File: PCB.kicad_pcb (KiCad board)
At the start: 2 copper layers, 88.5 x 156.5 mm, 48 parts, among them J1 Conn_01x04, J3 Screw_Terminal_01x05, J4 Screw_Terminal_01x05, K1 G5LE-1A_DC3, K2 G5LE-1A_DC3, K3 G5LE-1, K4 G5LE-1, K6 G5LE-1, K7 G5LE-1A_DC3, Q1 DMN65D8L-7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

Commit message: update the pcb
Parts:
- removed C2: 10uF, Capacitor_SMD:C_0603_1608Metric
- removed J1: Conn_01x04, Connector_PinHeader_2.54mm:PinHeader_1x04_P2.54mm_Horizontal
- removed J3, J4: Screw_Terminal_01x05, 1x5 screw conn:1935190
- added C_10uF_2: 10uF, Capacitor_SMD:C_0603_1608Metric, B.Cu at (62.0, 82.0)
- added J_LCDconn_1: Conn_01x04, Connector_PinHeader_2.54mm:PinHeader_1x04_P2.54mm_Horizontal, F.Cu at (65.5, 80.5)
- added J_VFDconnectors_2: Screw_Terminal_01x05, 1x5 screw conn:1935190, F.Cu at (93.2, 214.5)
- added J_VFDconnectors_3: Screw_Terminal_01x05, 1x5 screw conn:1935190, F.Cu at (121.5, 214.5)

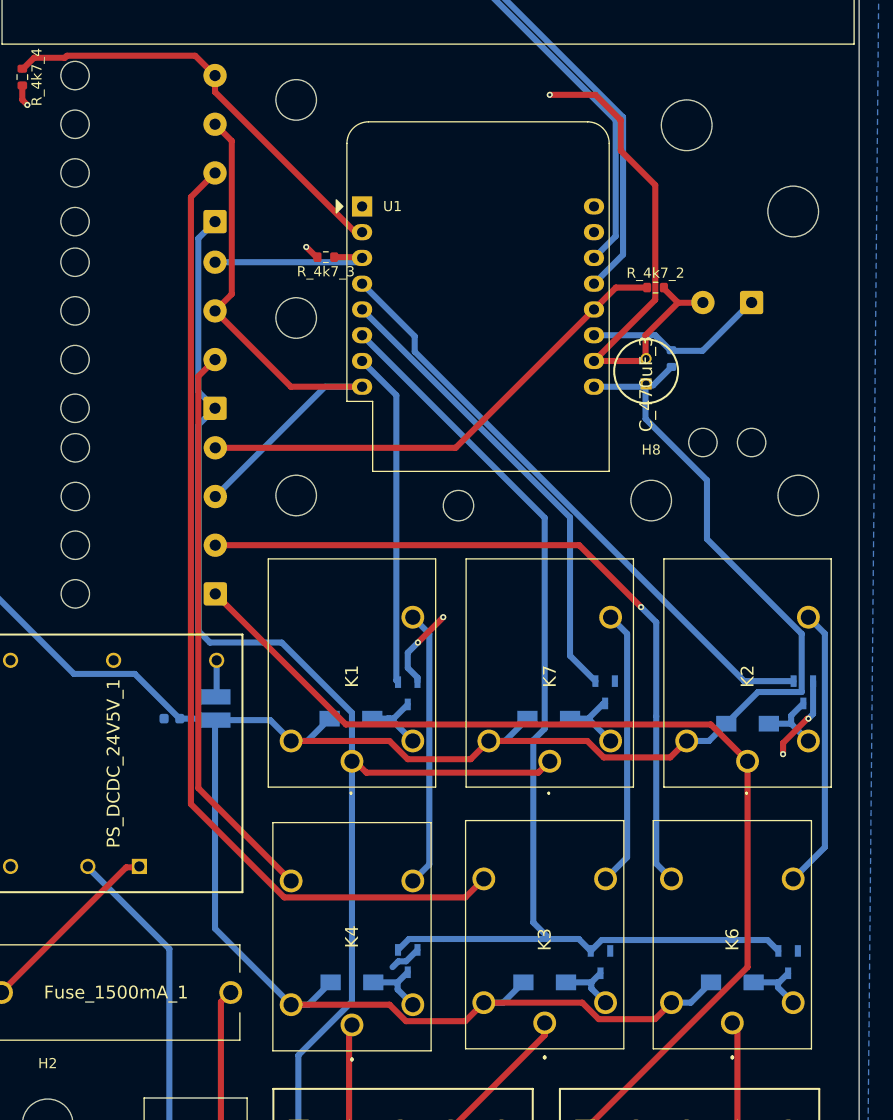
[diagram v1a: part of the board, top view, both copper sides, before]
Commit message: finalni uprava nazvu na pcb
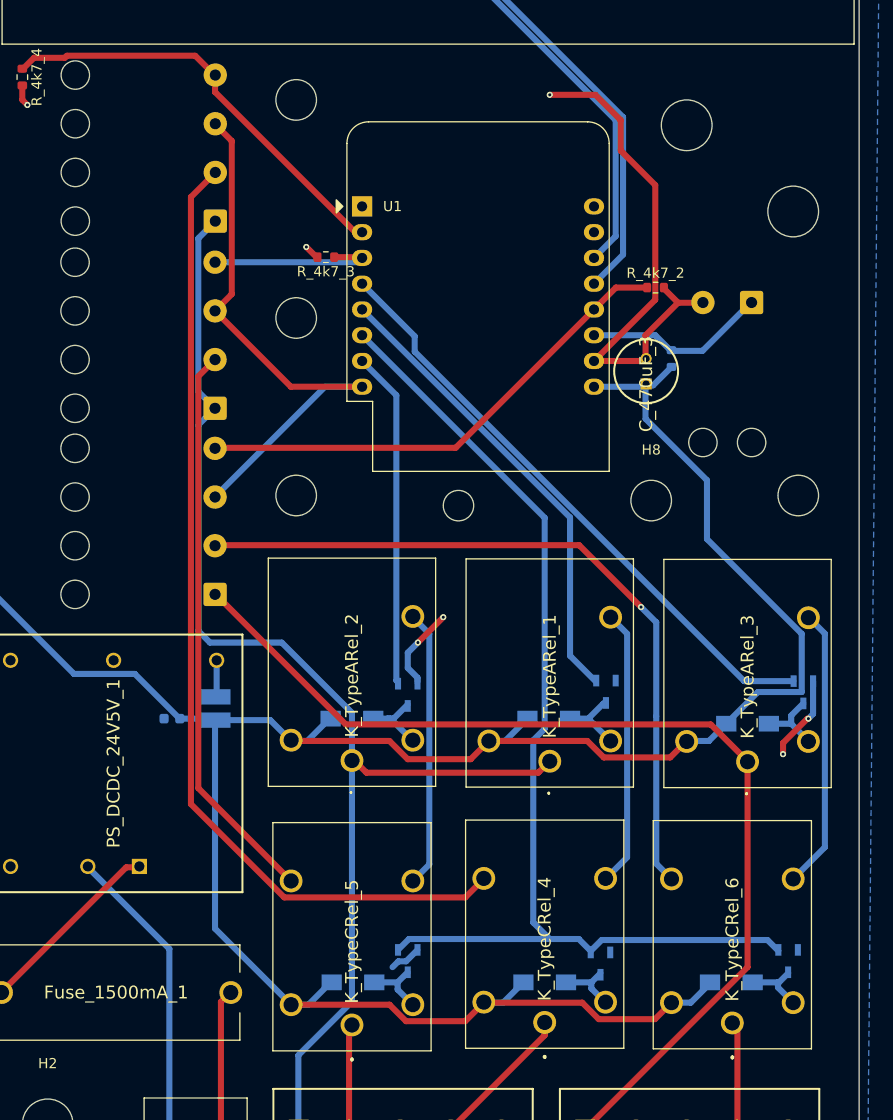
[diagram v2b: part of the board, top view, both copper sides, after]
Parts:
- removed D1, D2, D3, D4, D5, D6: SK16, schottky:DIOM5027X250N
- removed K1, K2, K7: G5LE-1A_DC3, type a relay:G5LE1A4DC5
- removed K3, K4, K6: G5LE-1, type c relay:G5LE1DC3
- removed Q1, Q2, Q3, Q4, Q5, Q6: DMN65D8L-7, mosfet:SOT96P240X115-3N
- removed SW1: Local DI0 (onoff), Connector_Wire:SolderWire-0.5sqmm_1x04_P4.8mm_D0.9mm_OD2.3mm_Relief
- removed SW3: Local DI2 (decspeed), Connector_Wire:SolderWire-0.5sqmm_1x04_P4.8mm_D0.9mm_OD2.3mm_Relief
- removed SW5: Local DI1 (incspeed), Connector_Wire:SolderWire-0.5sqmm_1x04_P4.8mm_D0.9mm_OD2.3mm_Relief
- added D_schottky_1: SK16, schottky:DIOM5027X250N, B.Cu at (117.5, 200.0)
- added D_schottky_2: SK16, schottky:DIOM5027X250N, B.Cu at (98.6, 200.0)
- added D_schottky_3: SK16, schottky:DIOM5027X250N, B.Cu at (135.9, 200.0)
- added D_schottky_4: SK16, schottky:DIOM5027X250N, B.Cu at (117.9, 174.0)
- added D_schottky_5: SK16, schottky:DIOM5027X250N, B.Cu at (98.5, 174.0)
- added D_schottky_6: SK16, schottky:DIOM5027X250N, B.Cu at (137.5, 174.5)
- added K_TypeARel_1: G5LE-1A_DC3, type a relay:G5LE1A4DC5, F.Cu at (118.0, 178.2)
- added K_TypeARel_2: G5LE-1A_DC3, type a relay:G5LE1A4DC5, F.Cu at (98.5, 178.1)
- added K_TypeARel_3: G5LE-1A_DC3, type a relay:G5LE1A4DC5, F.Cu at (137.5, 178.2)
- added K_TypeCRel_4: G5LE-1, type c relay:G5LE1DC3, F.Cu at (117.5, 203.9)
- added K_TypeCRel_5: G5LE-1, type c relay:G5LE1DC3, F.Cu at (98.5, 204.2)
- added K_TypeCRel_6: G5LE-1, type c relay:G5LE1DC3, F.Cu at (136.0, 204.0)
- added Q_NchMOSFET_1: DMN65D8L-7, mosfet:SOT96P240X115-3N, B.Cu at (123.0, 198.2)
- added Q_NchMOSFET_2: DMN65D8L-7, mosfet:SOT96P240X115-3N, B.Cu at (104.0, 197.9)
- added Q_NchMOSFET_3: DMN65D8L-7, mosfet:SOT96P240X115-3N, B.Cu at (141.5, 197.9)
- added Q_NchMOSFET_4: DMN65D8L-7, mosfet:SOT96P240X115-3N, B.Cu at (123.5, 171.3)
- added Q_NchMOSFET_5: DMN65D8L-7, mosfet:SOT96P240X115-3N, B.Cu at (104.0, 171.7)
- added Q_NchMOSFET_6: DMN65D8L-7, mosfet:SOT96P240X115-3N, B.Cu at (143.0, 171.4)
- added SW_DecSpeed_4: Local DI2 (decspeed), Connector_Wire:SolderWire-0.5sqmm_1x04_P4.8mm_D0.9mm_OD2.3mm_Relief, B.Cu at (85.0, 161.8)
- added SW_IncSpeed_3: Local DI1 (incspeed), Connector_Wire:SolderWire-0.5sqmm_1x04_P4.8mm_D0.9mm_OD2.3mm_Relief, B.Cu at (85.0, 143.4)
- added SW_OnOff_2: Local DI0 (onoff), Connector_Wire:SolderWire-0.5sqmm_1x04_P4.8mm_D0.9mm_OD2.3mm_Relief, B.Cu at (85.0, 125.0)
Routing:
- net Net-(D_schottky_5-A): track 0.00 -> 7.49 mm
- net Net-(D5-A): track 7.49 -> 0.00 mm
- net Net-(D_schottky_4-A): track 0.00 -> 7.19 mm
- net Net-(D4-A): track 7.19 -> 0.00 mm
- net Net-(D_schottky_6-A): track 0.00 -> 7.10 mm
- net Net-(D6-A): track 7.10 -> 0.00 mm
- net Net-(D_schottky_2-A): track 0.00 -> 6.64 mm
- net Net-(D2-A): track 6.64 -> 0.00 mm
- net Net-(D_schottky_3-A): track 0.00 -> 6.39 mm
- net Net-(D3-A): track 6.39 -> 0.00 mm
- net Net-(D_schottky_1-A): track 0.00 -> 6.35 mm
- net Net-(D1-A): track 6.35 -> 0.00 mm

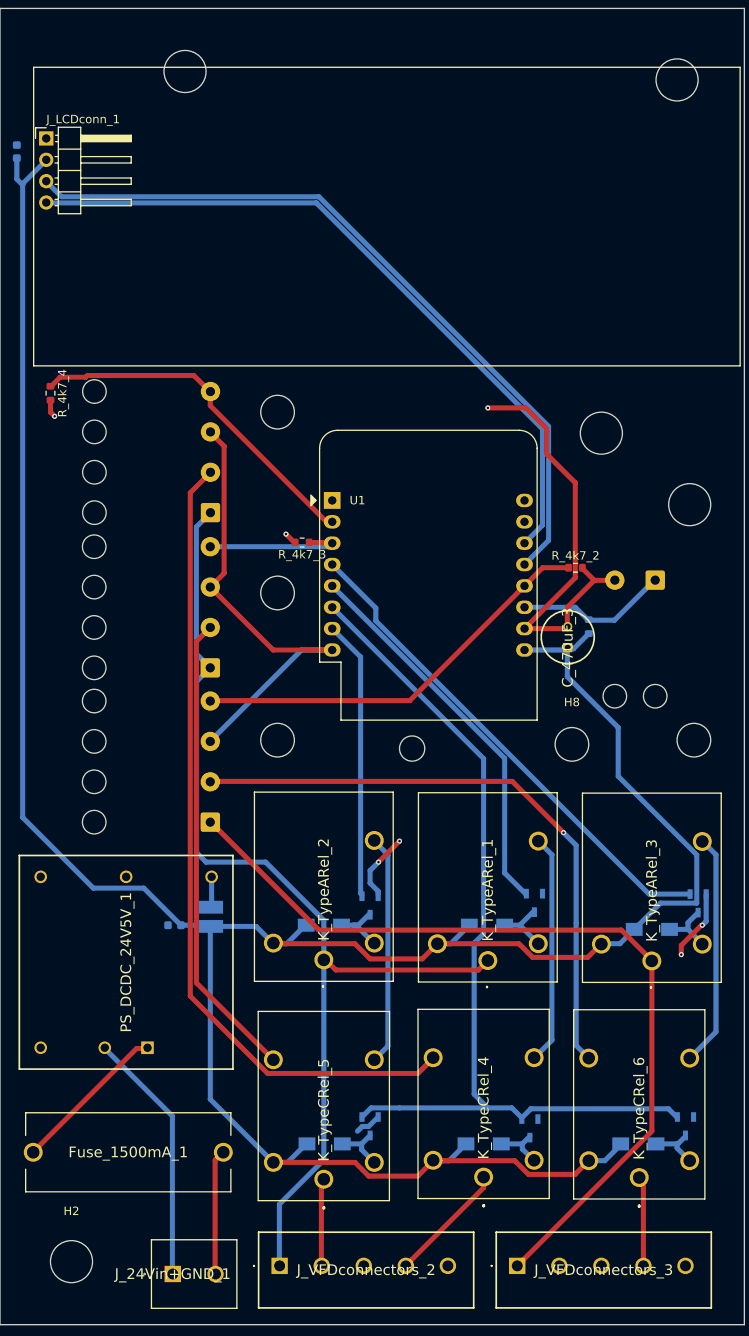
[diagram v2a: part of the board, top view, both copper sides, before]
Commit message: uprava textu na pcb aby byl videt i pod komponenty
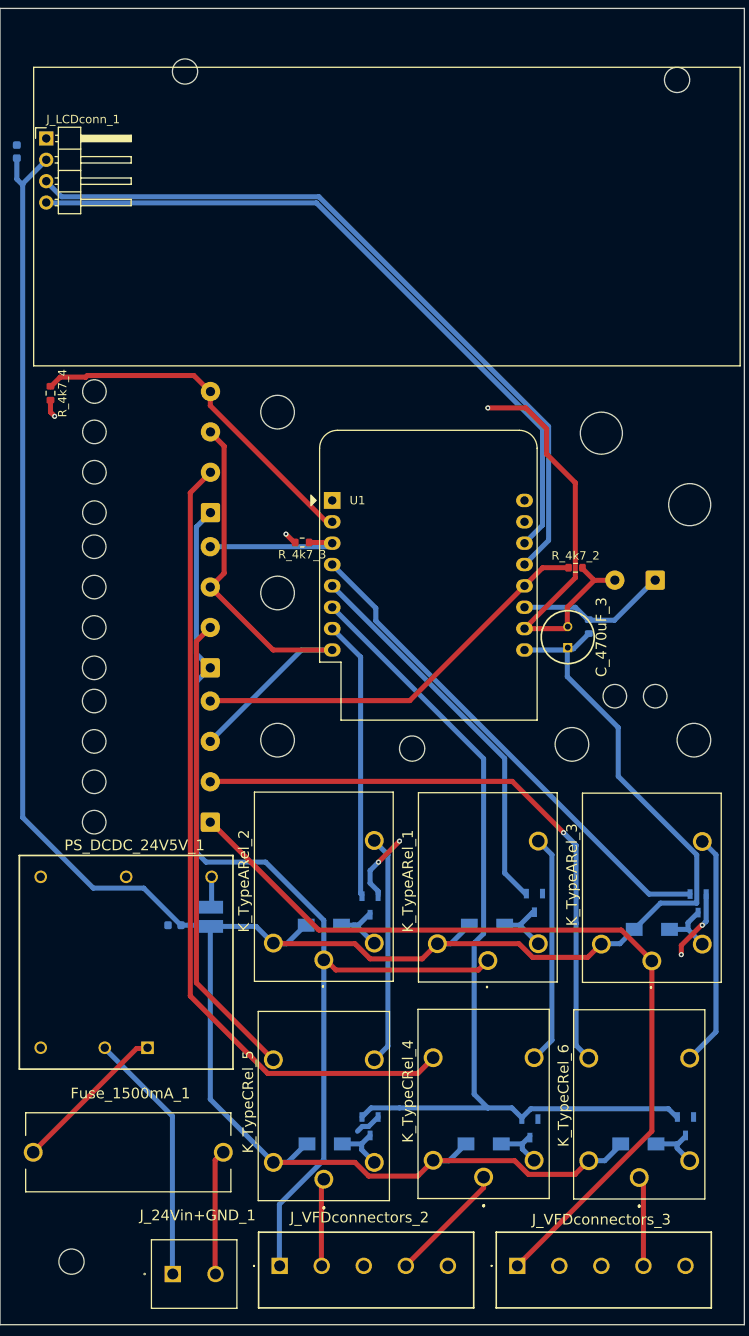
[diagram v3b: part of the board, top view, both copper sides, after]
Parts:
- H10, H11: footprint MountingHole:MountingHole_5mm -> MountingHole:MountingHole_3mm
- H2: footprint MountingHole:MountingHole_5mm -> MountingHole:MountingHole_3mm; moved to B.Cu
- H8: moved to B.Cu
- turned H2 to 180 degrees
- turned H8 to 180 degrees

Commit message: komponenty jsou rozlozeny spravne a zacinam delat cesty
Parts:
- removed D_schottky_1, D_schottky_2, D_schottky_3, D_schottky_4, D_schottky_5, D_schottky_6: SK16, schottky:DIOM5027X250N
- removed Q_NchMOSFET_1, Q_NchMOSFET_2, Q_NchMOSFET_3, Q_NchMOSFET_4, Q_NchMOSFET_5, Q_NchMOSFET_6: DMN65D8L-7, mosfet:SOT96P240X115-3N
- added D_sch_1: SK16, schottky:DIOM5027X250N, F.Cu at (119.0, 203.9)
- added D_sch_2: SK16, schottky:DIOM5027X250N, F.Cu at (100.1, 203.9)
- added D_sch_3: SK16, schottky:DIOM5027X250N, F.Cu at (137.0, 203.9)
- added D_sch_4: SK16, schottky:DIOM5027X250N, F.Cu at (118.5, 172.0)
- added D_sch_5: SK16, schottky:DIOM5027X250N, F.Cu at (99.0, 172.0)
- added D_sch_6: SK16, schottky:DIOM5027X250N, F.Cu at (138.1, 172.0)
- added Q_NchFET_1: DMN65D8L-7, mosfet:SOT96P240X115-3N, F.Cu at (125.1, 203.9)
- added Q_NchFET_2: DMN65D8L-7, mosfet:SOT96P240X115-3N, F.Cu at (106.1, 203.9)
- added Q_NchFET_3: DMN65D8L-7, mosfet:SOT96P240X115-3N, F.Cu at (143.1, 203.9)
- added Q_NchFET_4: DMN65D8L-7, mosfet:SOT96P240X115-3N, F.Cu at (124.4, 172.0)
- added Q_NchFET_5: DMN65D8L-7, mosfet:SOT96P240X115-3N, F.Cu at (105.1, 172.0)
- added Q_NchFET_6: DMN65D8L-7, mosfet:SOT96P240X115-3N, F.Cu at (144.1, 172.0)
- C_10uF_2, C_22uF_1, L_10uH_1, R_4k7_1: moved to F.Cu
- SW_DecSpeed_4, SW_IncSpeed_3, SW_OnOff_2: footprint Connector_Wire:SolderWire-0.5sqmm_1x04_P4.8mm_D0.9mm_OD2.3mm_Relief -> 1x4 screw conn:1935187; moved to F.Cu
- SW_LocRem_1: footprint Connector_Wire:SolderWire-0.5sqmm_1x02_P4.8mm_D0.9mm_OD2.3mm_Relief -> 1x2 screw conn:1729128; moved to F.Cu
- moved H10 167.5 mm to (307.0, 92.0)
- moved H11 167.5 mm to (248.5, 91.0)
- moved H2 167.5 mm to (235.0, 232.5)
- moved H1 136.6 mm to (266.5, 136.5)
- moved H3 136.6 mm to (228.0, 173.0)
- moved H4 136.6 mm to (277.0, 145.0)
- moved H5 136.6 mm to (277.5, 173.0)
- moved H6 136.6 mm to (228.0, 134.0)
- moved H7 136.6 mm to (244.0, 174.0)
- moved H8 136.6 mm to (263.0, 173.5)
- moved H9 136.6 mm to (228.0, 155.5)
- moved SW_IncSpeed_3 56.4 mm to (139.0, 127.2)
- moved SW_DecSpeed_4 17.0 mm to (70.0, 153.8)
- moved SW_OnOff_2 15.7 mm to (70.0, 129.5)
- moved C_22uF_1 14.1 mm to (94.8, 175.2), turned to 0 degrees
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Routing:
- net VCC: track 313.9 -> 0.00 mm
- net J3 24V: track 124.6 -> 0.00 mm
- net DO7: track 107.4 -> 0.00 mm
- net J4 24V: track 102.2 -> 0.00 mm
- net local DI0: track 96.7 -> 0.00 mm
- net SDA: track 89.4 -> 0.00 mm
- net SCL: track 84.6 -> 0.00 mm
- net GND: track 75.9 -> 0.00 mm, vias 7 -> 0
- net local DI2: track 72.5 -> 0.00 mm, vias 1 -> 0
- net DO5: track 59.7 -> 0.00 mm
- net MCU 3V3: track 56.3 -> 0.00 mm
- net local DI1: track 55.9 -> 0.00 mm
- net DO3: track 49.0 -> 0.00 mm
- net DO6: track 46.2 -> 0.00 mm
- net DO8: track 33.1 -> 0.00 mm
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- added copper zone on F.Cu, net GND
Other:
- board size 88.5 x 156.5 mm -> 89 x 156.5 mm

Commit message: zacal jsem wirovat draty a via
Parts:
- moved SW_DecSpeed_4 73.8 mm to (138.8, 127.0)
- moved SW_IncSpeed_3 72.9 mm to (70.2, 151.5)
- moved SW_LocRem_1 5.00 mm to (135.0, 135.8)
- moved R_4k7_2 3.04 mm to (118.1, 127.8)
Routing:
- net VCC: track 0.00 -> 335.5 mm, vias 0 -> 1
- net DO7: track 0.00 -> 122.8 mm
- net J3 24V: track 0.00 -> 109.7 mm
- net J4 24V: track 0.00 -> 94.6 mm
- net DO5: track 0.00 -> 80.5 mm
- net SDA: track 0.00 -> 77.8 mm
- net SCL: track 0.00 -> 73.0 mm
- net local DI2: track 0.00 -> 64.5 mm
- net DO6: track 0.00 -> 61.6 mm
- net local DI1: track 0.00 -> 47.8 mm
- net DO8: track 0.00 -> 47.5 mm
- net MCU 3V3: track 0.00 -> 43.0 mm
- net remote DI1: track 0.00 -> 33.5 mm
- net remote DI2: track 0.00 -> 32.9 mm
- net remote DI0: track 0.00 -> 32.7 mm
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
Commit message: dodelani wiringu pro desku v3 co ma vsechny komponenty nahore
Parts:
- moved H1 185.3 mm to (82.5, 158.0)
- moved H11 182.6 mm to (67.0, 71.2)
- moved H2 168.7 mm to (67.2, 214.2)
- moved H10 167.8 mm to (140.5, 71.5)
- moved H4 19.4 mm to (257.8, 143.0)
- moved C_470uF_3 0.94 mm to (120.2, 135.1)
- moved R_4k7_1 0.94 mm to (124.5, 132.6)
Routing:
- net local DI0: track 0.00 -> 89.7 mm
- net MCU 3V3: track 43.0 -> 104.4 mm
- net J3 24V: track 109.7 -> 143.0 mm, vias 0 -> 1
- net DO3: track 3.09 -> 31.1 mm
- net VCC: track 335.5 -> 361.2 mm, vias 1 -> 3
- net GND: track 4.56 -> 11.3 mm, vias 1 -> 4

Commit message: rewire dratu at je to nyni lepsi
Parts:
- moved H1 106.9 mm to (-23.2, 142.2)
- moved SW_DecSpeed_4 11.9 mm to (140.8, 115.2), turned to 180 degrees
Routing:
- net VCC: track 361.2 -> 333.8 mm, vias 3 -> 0
- net DO7: track 122.8 -> 140.2 mm, vias 0 -> 1
- net J4 24V: track 94.6 -> 107.2 mm
- net DO3: track 31.1 -> 19.1 mm
- net GND: track 11.3 -> 23.1 mm
- net J3 24V: track 143.0 -> 131.4 mm, vias 1 -> 0
- net MCU 3V3: track 104.4 -> 95.8 mm
- net local DI0: track 89.7 -> 83.3 mm
- net local DI2: track 64.5 -> 70.8 mm
- net DO0: track 29.6 -> 26.8 mm
- net DO6: track 61.6 -> 60.5 mm, vias 0 -> 1
- net DO8: track 47.5 -> 48.4 mm, vias 0 -> 1
- net SDA: track 77.8 -> 78.6 mm
- net SCL: track 73.0 -> 73.8 mm
- net VFD DI2: track 18.0 -> 17.3 mm
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
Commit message: deska je erc-error free
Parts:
- removed H3, H5, H6, H8: MountingHole, MountingHole:MountingHole_4mm
- removed H4: MountingHole, MountingHole:MountingHole_5mm
- removed H7: MountingHole, MountingHole:MountingHole_3mm
- moved H9 145.4 mm to (82.6, 158.3)
- moved H1 109.3 mm to (82.5, 114.8)
- moved H10 5.28 mm to (142.8, 66.8)
- moved H11 5.00 mm to (65.3, 66.5)
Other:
- board size 89 x 156.5 mm -> 89 x 160.1 mm
